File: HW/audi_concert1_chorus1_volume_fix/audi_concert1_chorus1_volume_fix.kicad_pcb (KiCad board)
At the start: 2 copper layers, 32.8 x 26.2 mm, 40 parts, among them CON1 I2C_to_TDA, CON2 USB, CON3 SPI_TO_PANEL, CON4 JLINK, U1 68HC05_PLCC, U2 AP1117-33, U3 STM32F103C8Tx, Y1 Crystal_GND24, Y2 Crystal_GND24

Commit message: move hw files
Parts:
- removed C1: 1uF, Capacitors_SMD.pretty:C_1206_HandSoldering
- removed R1: 100k, Resistors_SMD.pretty:R_0805_HandSoldering
- added U4: MAX809, TO_SOT_Packages_SMD.pretty:SOT-23, F.Cu at (175.5, 115.9)
- Y1: value Crystal_GND24 -> 32.768kHz
- Y2: value Crystal_GND24 -> 8MHz
- moved CON1 2.65 mm to (165.6, 95.5), turned to 0 degrees
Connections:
- CON2 pad 1: GND -> 5V
- CON2 pad 4: 5V -> GND
- R12 pad 1: /USB+ -> Net-(R12-Pad1)
- R13 pad 2: /USB- -> (no net)
- R14 pad 2: /USB+ -> Net-(R12-Pad1)
- U3 pad 32: /USB- -> (no net)
- U3 pad 33: /USB+ -> (no net)
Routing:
- net /USB-: track 9.25 -> 0.00 mm
- net (no net): track 0.00 -> 9.25 mm
- net /USB+: track 7.67 -> 0.00 mm
- net 5V: track 55.3 -> 48.3 mm
- net Net-(R12-Pad1): track 0.00 -> 6.17 mm
- net GND: track 114.0 -> 109.8 mm
- net /SDA_TO_TDA: track 28.1 -> 26.1 mm
- net /SCL_TO_TDA: track 25.7 -> 27.6 mm
- net /RESET: track 21.3 -> 20.7 mm

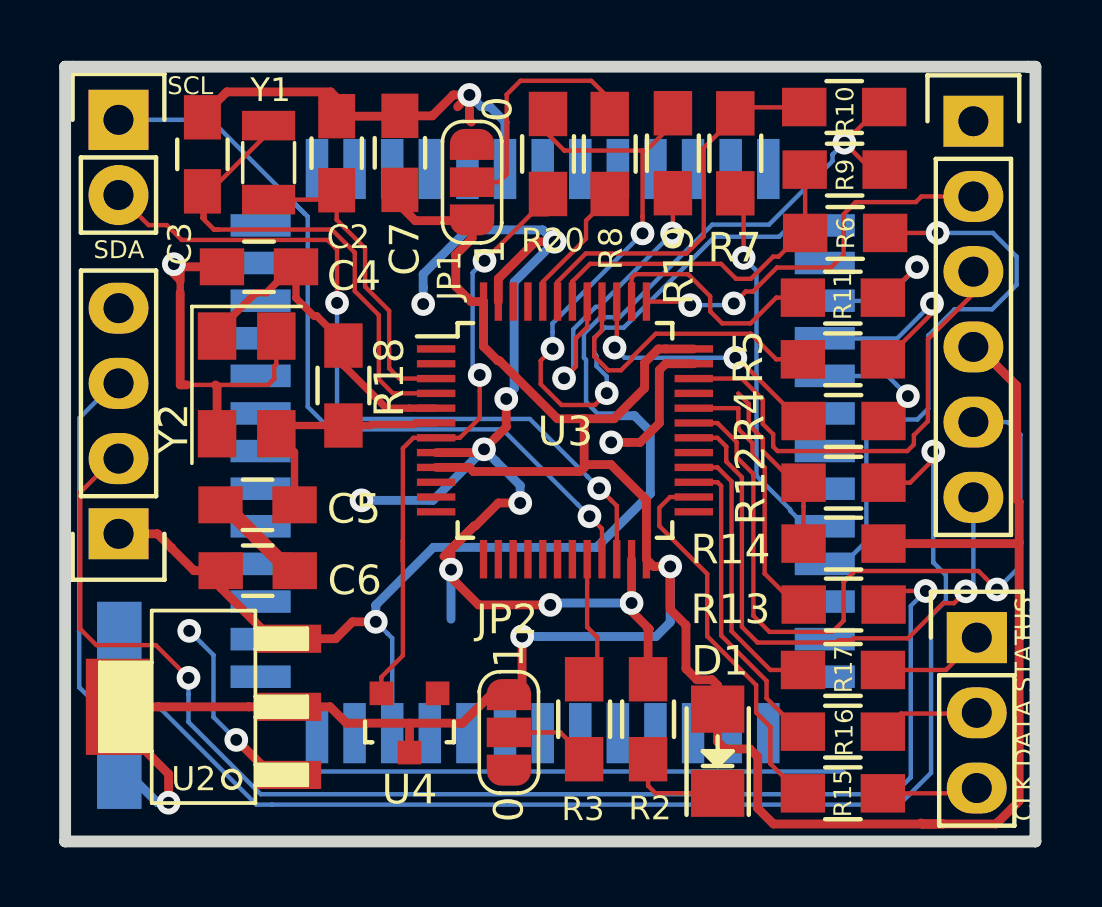
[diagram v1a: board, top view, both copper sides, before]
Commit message: HW part for GALA support
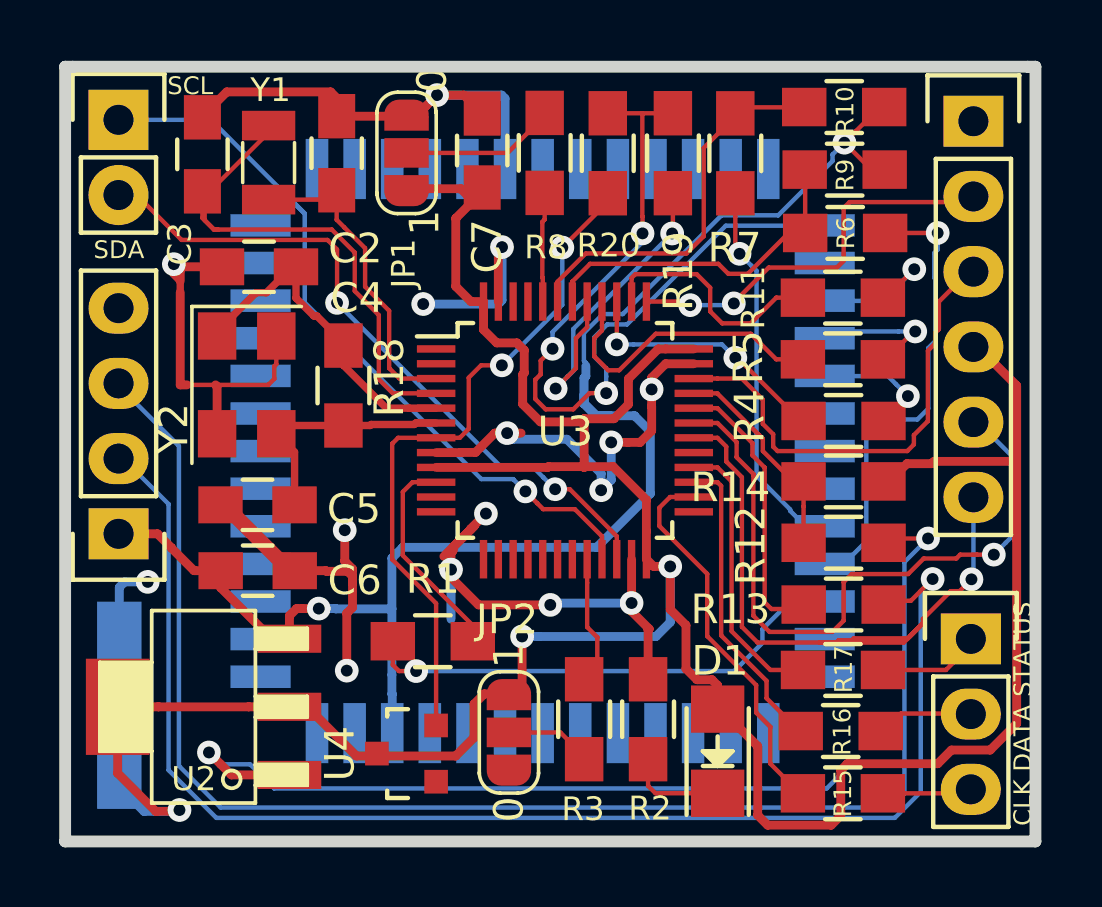
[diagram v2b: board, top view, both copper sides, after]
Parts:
- added R1: 1k, Resistors_SMD.pretty:R_0805_HandSoldering, F.Cu at (176.2, 113.1)
- D1: value red -> LED
- moved C7 2.78 mm to (177.9, 96.6)
- moved JP1 2.42 mm to (175.4, 96.6)
- moved R8 2.20 mm to (180.0, 96.6)
- moved R14 2.10 mm to (190.1, 107.7)
- moved R12 2.03 mm to (190.1, 109.8)
- moved R20 2.02 mm to (182.2, 96.6)
- moved U4 1.04 mm to (175.4, 116.9), turned to 90 degrees
- moved CON3 0.21 mm to (194.4, 113.0)
- moved R16 0.08 mm to (190.0, 116.2)
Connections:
- R12 pad 1: Net-(R12-Pad1) -> /USB+
- R13 pad 2: (no net) -> /USB-
- R14 pad 2: Net-(R12-Pad1) -> /USB+
- U1 pad 23: (no net) -> /GALA
- U3 pad 10: (no net) -> Net-(R1-Pad2)
- U3 pad 32: (no net) -> /USB-
- U3 pad 33: (no net) -> /USB+
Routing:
- net /GALA: track 0.00 -> 16.7 mm, vias 0 -> 1
- net /USB-: track 0.00 -> 9.40 mm
- net (no net): track 9.25 -> 0.00 mm
- net Net-(R1-Pad2): track 0.00 -> 7.28 mm
- net /USB+: track 0.00 -> 7.26 mm
- net Net-(R12-Pad1): track 6.17 -> 0.00 mm
- net Net-(CON2-Pad3): track 55.3 -> 49.5 mm
- net /TX: track 19.3 -> 23.5 mm
- net /SCL_FROM_MOTO: track 19.6 -> 15.6 mm
- net 5V: track 48.3 -> 52.3 mm
- net /BOOT0: track 8.40 -> 5.28 mm
- net GND: track 109.8 -> 106.9 mm, vias 14 -> 16
- net /SDA_TO_TDA: track 26.1 -> 23.4 mm
- net /RESET: track 20.7 -> 23.2 mm
- net 3V3: track 101.0 -> 103.2 mm
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
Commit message: hw, silkscreen positions
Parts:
- renumbered JP1 to BOOT0, JP2 to BOOT1
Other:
- board text added: "5V|D-|D+|GND"
- board text added: "CL|DA|ST"
- board text added: "TX|RX|3v|IO|CL|GD"
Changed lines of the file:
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@@
-(kicad_pcb (version 20171130) (host pcbnew 5.1.0-unknown-ff73f69~82~ubuntu16.04.1)
+(kicad_pcb (version 20190331) (host pcbnew 5.1.0-unknown-8985bad~82~ubuntu16.04.1)
   (general
     (thickness 1.6)
-    (drawings 14)
+    (drawings 20)
     (tracks 689)
     (zones 0)
@@
     (pad 2 smd rect (at -9.525 1.27) (size 2.032 0.762) (layers B.Cu B.Paste B.Mask))
     (pad 1 smd rect (at -9.525 0) (size 2.032 0.762) (layers B.Cu B.Paste B.Mask))
+    (model /home/nail/src/kicad/modules/packages3d/pth_plcc/plcc52_pth-skt_smd.wrl
+      (offset (xyz 0 0 -1.5))
+      (scale (xyz 1 1 1))
+      (rotate (xyz 180 0 0))
+    )
   )
   (module ab2_sot.mod:AB2_SOT223 (layer F.Cu)
@@
     (tags "capacitor 0805")
     (attr smd)
-    (fp_text reference C2 (at -3.22072 0.62992 180) (layer F.SilkS)
+    (fp_text reference C2 (at -2.9464 0.6477 180) (layer F.SilkS)
       (effects (font (size 1 1) (thickness 0.15)))
     )
@@
     (tags "Tantal Cap. , Size A, EIA-3216, Hand Soldering,")
     (attr smd)
-    (fp_text reference C8 (at -0.20066 3.0988 90) (layer B.SilkS)
+    (fp_text reference C8 (at -3.175 1.95072 90) (layer B.SilkS)
       (effects (font (size 1 1) (thickness 0.15)) (justify mirror))
     )
@@
     (fp_line (start 2.60096 1.19888) (end -2.60096 1.19888) (layer B.SilkS) (width 0.15))
     (fp_line (start -2.60096 -1.19888) (end 2.60096 -1.19888) (layer B.SilkS) (width 0.15))
-    (fp_text user + (at -4.59994 1.80086 90) (layer B.SilkS)
+    (fp_text user + (at -3.87604 2.91084 90) (layer B.SilkS)
       (effects (font (size 1 1) (thickness 0.15)) (justify mirror))
     )
@@
     (pad 2 smd rect (at 1.99898 0 90) (size 2.99974 1.50114) (layers B.Cu B.Paste B.Mask)
       (net 2 GND))
-    (model Capacitors_Tantalum_SMD.3dshapes/TantalC_SizeA_EIA-3216_HandSoldering.wrl
-      (at (xyz 0 0 0))
-      (scale (xyz 1 1 1))
-      (rotate (xyz 0 0 180))
+    (model ${KISYS3DMOD}/Capacitor_Tantalum_SMD.3dshapes/CP_EIA-3216-18_Kemet-A.wrl
+      (at (xyz 0 0 0))
+      (scale (xyz 1 1 1))
+      (rotate (xyz 0 0 0))
     )
   )
@@
     (tags "solder jumper open")
     (attr virtual)
-    (fp_text reference JP2 (at 3.81 -0.0635 180) (layer F.SilkS)
+    (fp_text reference BOOT1 (at 3.5052 2.2479 180) (layer F.SilkS)
       (effects (font (size 1 1) (thickness 0.15)))
     )
@@
       (effects (font (size 1 1) (thickness 0.15)))
     )
-    (fp_text user 1 (at 2.6 0 90) (layer F.SilkS)
-      (effects (font (size 1 1) (thickness 0.15)))
-    )
-    (fp_text user 0 (at -2.6 0 90) (layer F.SilkS)
+    (fp_text user 1 (at 2.63144 0.74168 90) (layer F.SilkS)
+      (effects (font (size 1 1) (thickness 0.15)))
+    )
+    (fp_text user 0 (at -2.42824 1.01854 90) (layer F.SilkS)
       (effects (font (size 1 1) (thickness 0.15)))
     )
@@
     (tags "resistor 0805")
     (attr smd)
-    (fp_text reference R14 (at 3.8189 -0.2032) (layer F.SilkS)
+    (fp_text reference R14 (at 2.97054 0.14986 90) (layer F.SilkS)
       (effects (font (size 1 1) (thickness 0.15)))
     )
@@
     (tags "resistor 0805")
     (attr smd)
-    (fp_text reference R4 (at -3.1712 -0.16764 90) (layer F.SilkS)
+    (fp_text reference R4 (at -3.52934 -0.28448 90) (layer F.SilkS)
       (effects (font (size 1 1) (thickness 0.15)))
     )
@@
     (tags "resistor 0805")
     (attr smd)
-    (fp_text reference R5 (at 3.19152 0.07112 270) (layer F.SilkS)
+    (fp_text reference R5 (at 2.97434 -0.02286 270) (layer F.SilkS)
       (effects (font (size 1 1) (thickness 0.15)))
     )
@@
     (tags "resistor 0805")
     (attr smd)
-    (fp_text reference R7 (at 3.18896 0.0254) (layer F.SilkS)
+    (fp_text reference R7 (at 3.07468 -0.2032) (layer F.SilkS)
       (effects (font (size 1 1) (thickness 0.15)))
     )
@@
     (tags "resistor 0805")
     (attr smd)
-    (fp_text reference R11 (at -3.02768 -0.00254 90) (layer F.SilkS)
-      (effects (font (size 0.8 0.8) (thickness 0.1)))
+    (fp_text reference R11 (at -3.80492 -0.01778 90) (layer F.SilkS)
+      (effects (font (size 1 1) (thickness 0.15)))
     )
     (fp_text value 1k (at 0.02794 -0.02286) (layer F.Fab)
@@
     (tags "capacitor 0805")
     (attr smd)
-    (fp_text reference C3 (at 3.0226 0.762 90) (layer F.SilkS)
+    (fp_text reference C3 (at 3.10642 0.87884 90) (layer F.SilkS)
       (effects (font (size 0.8 0.8) (thickness 0.125)))
     )
@@
     (tags "capacitor 0805")
     (attr smd)
-    (fp_text reference C4 (at -3.31946 -1.0541 180) (layer F.SilkS)
+    (fp_text reference C4 (at -3.20008 -0.56134 180) (layer F.SilkS)
       (effects (font (size 1 1) (thickness 0.15)))
     )
@@
     (tags "capacitor 0805")
     (attr smd)
-    (fp_text reference C6 (at 3.2766 0.3302 -180) (layer F.SilkS)
+    (fp_text reference C6 (at 3.2131 -0.59182 -180) (layer F.SilkS)
       (effects (font (size 1 1) (thickness 0.15)))
     )
@@
     (tags "solder jumper open")
     (attr virtual)
-    (fp_text reference JP1 (at 3.7338 0.09906 90) (layer F.SilkS)
+    (fp_text reference BOOT0 (at 4.20878 0.30226 90) (layer F.SilkS)
       (effects (font (size 0.8 0.8) (thickness 0.125)))
     )
@@
     (fp_line (start 1.4 1) (end -1.4 1) (layer F.SilkS) (width 0.12))
     (fp_line (start -2.05 0.3) (end -2.05 -0.3) (layer F.SilkS) (width 0.12))
-    (fp_text user 0 (at -2.4638 -0.8636 90) (layer F.SilkS)
-      (effects (font (size 1 1) (thickness 0.15)))
+    (fp_text user 0 (at -2.2225 -1.08204 90) (layer F.SilkS)
+      (effects (font (size 0.8 0.8) (thickness 0.1)))
     )
     (fp_text user 1 (at 2.3576 -0.6096 270) (layer F.SilkS)
@@
     (tags "resistor 0805")
     (attr smd)
-    (fp_text reference R12 (at -3.1331 0.0889 90) (layer F.SilkS)
+    (fp_text reference R12 (at -3.59156 0.55626 90) (layer F.SilkS)
       (effects (font (size 1 1) (thickness 0.15)))
     )
@@
     (tags "resistor 0805")
     (attr smd)
-    (fp_text reference R13 (at 3.8227 -0.1651) (layer F.SilkS)
+    (fp_text reference R13 (at 3.79476 -0.52324) (layer F.SilkS)
       (effects (font (size 1 1) (thickness 0.15)))
     )
@@
     (tags "SMD SMT crystal")
     (attr smd)
-    (fp_text reference Y2 (at 1.4722 2.4732 270) (layer F.SilkS)
+    (fp_text reference Y2 (at 0.0371 -0.01854) (layer F.SilkS)
       (effects (font (size 1 1) (thickness 0.15)))
     )
@@
     (tags "resistor 0805")
     (attr smd)
-    (fp_text reference R1 (at 0 -2.1) (layer F.SilkS)
+    (fp_text reference R1 (at -1.4605 -1.61036) (layer F.SilkS)
       (effects (font (size 1 1) (thickness 0.15)))
     )
@@
       (rotate (xyz 0 0 0))
     )
+  )
+  (gr_text CL|DA|ST (at 191.81318 115.6462 270) (layer B.SilkS)
+    (effects (font (size 1 1) (thickness 0.15)) (justify mirror))
+  )
+  (gr_text TX|RX|3v|IO|CL|GD (at 191.77508 101.4984 270) (layer B.SilkS)
+    (effects (font (size 1 1) (thickness 0.15)) (justify mirror))
+  )
+  (gr_text 5V|D-|D+|GND (at 168.1861 105.68432 270) (layer B.SilkS)
+    (effects (font (size 1 1) (thickness 0.15)) (justify mirror))
+  )
+  (gr_text SDA (at 168.70934 97.60712) (layer B.SilkS)
+    (effects (font (size 1 1) (thickness 0.15)) (justify mirror))
+  )
+  (gr_text SCL (at 168.69156 95.3135) (layer B.SilkS)
+    (effects (font (size 1 1) (thickness 0.15)) (justify mirror))
+  )
+  (gr_text 5V|D-|D+|GND (at 167.5638 105.41 90) (layer F.SilkS)
+    (effects (font (size 1 0.8) (thickness 0.15)))
   )
   (gr_text v2.0 (at 180.3781 111.4552) (layer B.SilkS)
@@
   (segment (start 188.7436 101.5238) (end 187.8436 101.5238) (width 0.15) (layer F.Cu) (net 31) (status 10))
   (segment (start 185.156419 100.731899) (end 183.083301 100.731899) (width 0.15) (layer F.Cu) (net 31))
-  (segment (start 186.974411 102.392989) (end 186.018193 102.392989) (width 0.15) (layer F.Cu) (net 31))
+  (segment (start 186.97194 102.38994) (end 186.015722 102.38994) (width 0.15) (layer F.Cu) (net 31))
   (segment (start 187.8436 101.5238) (end 186.974411 102.392989) (width 0.15) (layer F.Cu) (net 31))
   (segment (start 185.612401 101.187881) (end 185.156419 100.731899) (width 0.15) (layer F.Cu) (net 31))

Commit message: pcb update
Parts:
- moved C8 66.2 mm to (103.4, 92.7)
- moved CON1 66.2 mm to (103.4, 72.9)
- moved Y1 66.2 mm to (108.5, 74.4)
- moved BOOT0 66.2 mm to (113.1, 74.0)
- moved BOOT1 66.2 mm to (116.6, 93.6)
- moved C2 66.2 mm to (110.8, 74.0)
- moved C4 66.2 mm to (108.1, 77.9)
- moved C5 66.2 mm to (108.1, 85.9)
- moved C6 66.2 mm to (108.1, 88.1)
- moved C7 66.2 mm to (115.7, 73.9)
- moved R1 66.2 mm to (114.0, 90.5)
- moved R11 66.2 mm to (127.9, 78.9)
- moved R13 66.2 mm to (127.9, 89.3)
- moved R15 66.2 mm to (127.9, 95.7)
- moved R18 66.2 mm to (111.0, 81.9)
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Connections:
- BOOT0 pad 1: GND -> (no net)
- BOOT0 pad 2: /BOOT0 -> (no net)
- BOOT0 pad 3: 3V3 -> (no net)
- BOOT1 pad 1: GND -> (no net)
- BOOT1 pad 2: /BOOT1 -> (no net)
- BOOT1 pad 3: 3V3 -> (no net)
- C2 pad 1: /OSC32IN -> (no net)
- C2 pad 2: GND -> (no net)
- C3 pad 1: GND -> (no net)
- C3 pad 2: /OSC32OUT -> (no net)
- C4 pad 1: /OSCIN -> (no net)
- C4 pad 2: GND -> (no net)
- C5 pad 1: GND -> (no net)
- C5 pad 2: /OSCOUT -> (no net)
- C6 pad 1: 5V -> (no net)
- C6 pad 2: GND -> (no net)
- C7 pad 1: 3V3 -> (no net)
- C7 pad 2: GND -> (no net)
- C8 pad 1: 3V3 -> (no net)
- C8 pad 2: GND -> (no net)
- CON1 pad 1: /SCL_TO_TDA -> (no net)
- CON1 pad 2: /SDA_TO_TDA -> (no net)
- CON2 pad 1: 5V -> (no net)
- CON2 pad 2: Net-(CON2-Pad2) -> (no net)
- CON2 pad 3: Net-(CON2-Pad3) -> (no net)
- CON2 pad 4: GND -> (no net)
- CON3 pad 1: /STATUS_TO_PANEL -> (no net)
- CON3 pad 2: /DATA_TO_PANEL -> (no net)
- CON3 pad 3: /CLOCK_TO_PANEL -> (no net)
- CON4 pad 1: GND -> (no net)
- CON4 pad 2: /SWDCLK -> (no net)
- CON4 pad 3: /SWDIO -> (no net)
- CON4 pad 4: 3V3 -> (no net)
- CON4 pad 5: /RX -> (no net)
- CON4 pad 6: /TX -> (no net)
- D1 pad 1: Net-(D1-Pad1) -> (no net)
- D1 pad 2: 3V3 -> (no net)
- R1 pad 1: /GALA -> (no net)
- R1 pad 2: Net-(R1-Pad2) -> (no net)
- R10 pad 1: Net-(R10-Pad1) -> (no net)
- R10 pad 2: 5V -> (no net)
- R11 pad 1: Net-(R11-Pad1) -> (no net)
- R11 pad 2: /STATUS_FROM_MCU -> (no net)
- R12 pad 1: /USB+ -> (no net)
- R12 pad 2: Net-(CON2-Pad3) -> (no net)
- R13 pad 1: Net-(CON2-Pad2) -> (no net)
- R13 pad 2: /USB- -> (no net)
- R14 pad 1: 3V3 -> (no net)
- R14 pad 2: /USB+ -> (no net)
- R15 pad 1: /CLOCK_TO_PANEL -> (no net)
- R15 pad 2: Net-(R15-Pad2) -> (no net)
- R16 pad 1: /DATA_TO_PANEL -> (no net)
- R16 pad 2: Net-(R16-Pad2) -> (no net)
- R17 pad 1: /STATUS_TO_PANEL -> (no net)
- R17 pad 2: Net-(R17-Pad2) -> (no net)
- R18 pad 1: /OSCOUT -> (no net)
- R18 pad 2: /OSCIN -> (no net)
- R19 pad 1: /RESET_KA -> (no net)
- R19 pad 2: Net-(R19-Pad2) -> (no net)
- R2 pad 1: GND -> (no net)
- R2 pad 2: Net-(D1-Pad1) -> (no net)
- R20 pad 1: /RESET_KA -> (no net)
- R20 pad 2: /RESET -> (no net)
- R3 pad 1: Net-(R3-Pad1) -> (no net)
- R3 pad 2: /BOOT1 -> (no net)
- R4 pad 1: Net-(R4-Pad1) -> (no net)
- R4 pad 2: /CLOCK_FROM_MCU -> (no net)
- R5 pad 1: /DATA_FROM_MCU -> (no net)
- R5 pad 2: Net-(R5-Pad2) -> (no net)
- R6 pad 1: Net-(R6-Pad1) -> (no net)
- R6 pad 2: /SCL_FROM_MOTO -> (no net)
- R7 pad 1: Net-(R10-Pad1) -> (no net)
- R7 pad 2: /SDA_FROM_MOTO -> (no net)
- R8 pad 1: Net-(R8-Pad1) -> (no net)
- R8 pad 2: /BOOT0 -> (no net)
- R9 pad 1: 5V -> (no net)
- R9 pad 2: Net-(R6-Pad1) -> (no net)
- U1 pad 10: 5V -> (no net)
- U1 pad 23: /GALA -> (no net)
- U1 pad 24: /SCL_FROM_MOTO -> (no net)
- U1 pad 25: /SDA_FROM_MOTO -> (no net)
- U1 pad 29: /CLOCK_FROM_MCU -> (no net)
- U1 pad 30: /DATA_FROM_MCU -> (no net)
- U1 pad 31: /STATUS_FROM_MCU -> (no net)
- U1 pad 33: /RESET_KA -> (no net)
- U1 pad 41: GND -> (no net)
- U2 pad 1: GND -> (no net)
- U2 pad 2: 3V3 -> (no net)
- U2 pad 3: 5V -> (no net)
- U3 pad 10: Net-(R1-Pad2) -> (no net)
- U3 pad 20: Net-(R3-Pad1) -> (no net)
- U3 pad 21: /SCL_TO_TDA -> (no net)
- U3 pad 22: /SDA_TO_TDA -> (no net)
- U3 pad 23: GND -> (no net)
- U3 pad 24: 3V3 -> (no net)
- U3 pad 26: Net-(R15-Pad2) -> (no net)
- U3 pad 27: Net-(R16-Pad2) -> (no net)
- U3 pad 28: Net-(R17-Pad2) -> (no net)
- U3 pad 3: /OSC32IN -> (no net)
- U3 pad 30: /TX -> (no net)
- U3 pad 31: /RX -> (no net)
- U3 pad 32: /USB- -> (no net)
- U3 pad 33: /USB+ -> (no net)
- U3 pad 34: /SWDIO -> (no net)
- U3 pad 35: GND -> (no net)
- U3 pad 36: 3V3 -> (no net)
- U3 pad 37: /SWDCLK -> (no net)
- U3 pad 38: Net-(R11-Pad1) -> (no net)
- U3 pad 39: Net-(R4-Pad1) -> (no net)
- U3 pad 4: /OSC32OUT -> (no net)
- U3 pad 40: Net-(R5-Pad2) -> (no net)
- U3 pad 41: Net-(R19-Pad2) -> (no net)
- U3 pad 42: Net-(R6-Pad1) -> (no net)
- U3 pad 43: Net-(R10-Pad1) -> (no net)
- U3 pad 44: Net-(R8-Pad1) -> (no net)
- U3 pad 47: GND -> (no net)
- U3 pad 48: 3V3 -> (no net)
- U3 pad 5: /OSCIN -> (no net)
- U3 pad 6: /OSCOUT -> (no net)
- U3 pad 7: /RESET -> (no net)
- U3 pad 8: GND -> (no net)
- U3 pad 9: 3V3 -> (no net)
- U4 pad 1: GND -> (no net)
- U4 pad 2: /RESET -> (no net)
- U4 pad 3: 3V3 -> (no net)
- Y1 pad 1: /OSC32IN -> (no net)
- Y1 pad 2: /OSC32OUT -> (no net)
- Y2 pad 1: /OSCIN -> (no net)
- Y2 pad 2: GND -> (no net)
- Y2 pad 3: /OSCOUT -> (no net)
- Y2 pad 4: GND -> (no net)
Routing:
- net (no net): track 0.00 -> 796.3 mm, vias 0 -> 45
- net GND: track 106.9 -> 0.00 mm, vias 16 -> 0
- net 3V3: track 103.2 -> 0.00 mm, vias 3 -> 0
- net 5V: track 52.3 -> 0.00 mm, vias 2 -> 0
- net Net-(CON2-Pad3): track 49.5 -> 0.00 mm, vias 1 -> 0
- net Net-(CON2-Pad2): track 47.2 -> 0.00 mm, vias 1 -> 0
- net /RESET_KA: track 27.5 -> 0.00 mm, vias 3 -> 0
- net /SCL_TO_TDA: track 25.4 -> 0.00 mm, vias 1 -> 0
- net /TX: track 23.5 -> 0.00 mm, vias 1 -> 0
- net /RX: track 23.5 -> 0.00 mm, vias 1 -> 0
- net /SDA_TO_TDA: track 23.4 -> 0.00 mm, vias 2 -> 0
- net /RESET: track 23.2 -> 0.00 mm, vias 2 -> 0
- net /OSC32OUT: track 18.1 -> 0.00 mm
- net /GALA: track 16.7 -> 0.00 mm, vias 1 -> 0
- net /SWDIO: track 16.0 -> 0.00 mm
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- added copper zone on B.Cu, net (none)
- added copper zone on F.Cu, net (none)
- removed copper zone on B.Cu, net GND
- removed copper zone on F.Cu, net GND
